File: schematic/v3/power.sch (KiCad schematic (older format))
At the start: 17 parts, among them IC1 MCP73831/2, J13 LIPO_BAT, SW1 RS stock no. 448-0747, U1 TLV71333PDBV, U3 TLV71333PDBV

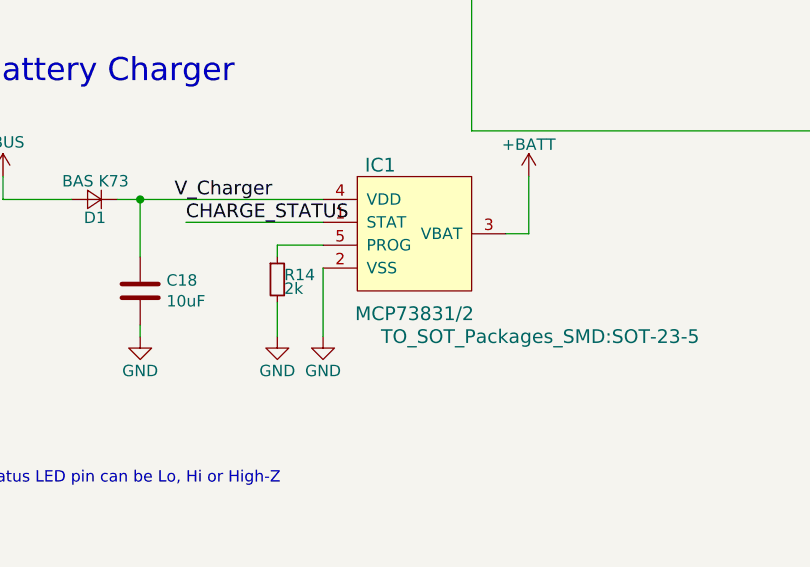
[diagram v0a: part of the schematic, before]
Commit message: Add 4.7uF caps around battery charger
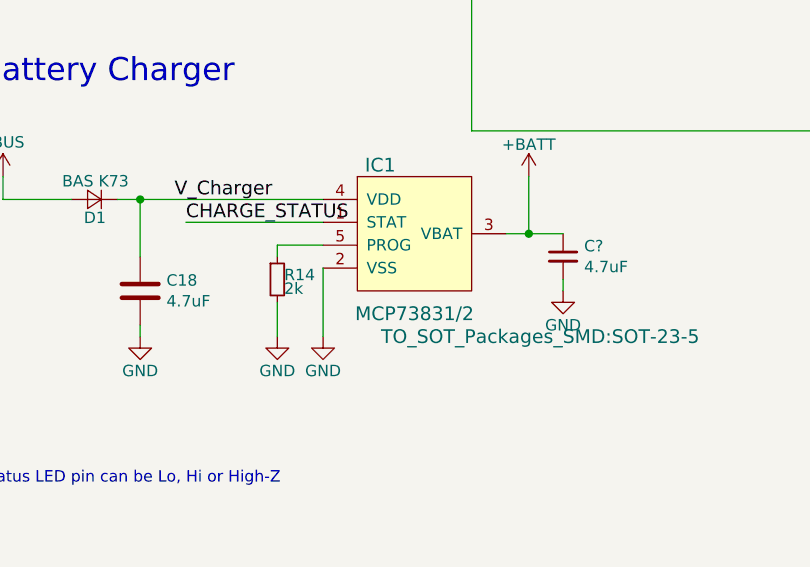
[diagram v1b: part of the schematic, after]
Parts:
- added C?: 4.7uF, symbol Device:C_Small
- C18: value 10uF -> 4.7uF
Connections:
- wire segments 75 -> 77
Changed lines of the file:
@@
 P 2650 4050
 F 0 "C18" H 2765 4096 50  0000 L CNN
-F 1 "10uF" H 2765 4005 50  0000 L CNN
+F 1 "4.7uF" H 2765 4005 50  0000 L CNN
 F 2 "" H 2688 3900 50  0001 C CNN
 F 3 "~" H 2650 4050 50  0001 C CNN
@@
 	4650 1900 4500 1900
 Connection ~ 6850 1850
+$Comp
+L Device:C_Small C?
+U 1 1 5BFBB945
+P 4500 3900
+F 0 "C?" H 4592 3946 50  0000 L CNN
+F 1 "4.7uF" H 4592 3855 50  0000 L CNN
+F 2 "" H 4500 3900 50  0001 C CNN
+F 3 "~" H 4500 3900 50  0001 C CNN
+	1    4500 3900
+	1    0    0    -1
+$EndComp
+Wire Wire Line
+	4350 3800 4500 3800
+Connection ~ 4350 3800
+$Comp
+L gps_node-rescue:GND-power #PWR?
+U 1 1 5BFBD3F1
+P 4500 4050
+F 0 "#PWR?" H 4500 3800 50  0001 C CNN
+F 1 "GND" H 4500 3900 50  0000 C CNN
+F 2 "" H 4500 4050 50  0001 C CNN
+F 3 "" H 4500 4050 50  0001 C CNN
+	1    4500 4050
+	1    0    0    -1
+$EndComp
+Wire Wire Line
+	4500 4050 4500 4000
 $EndSCHEMATC

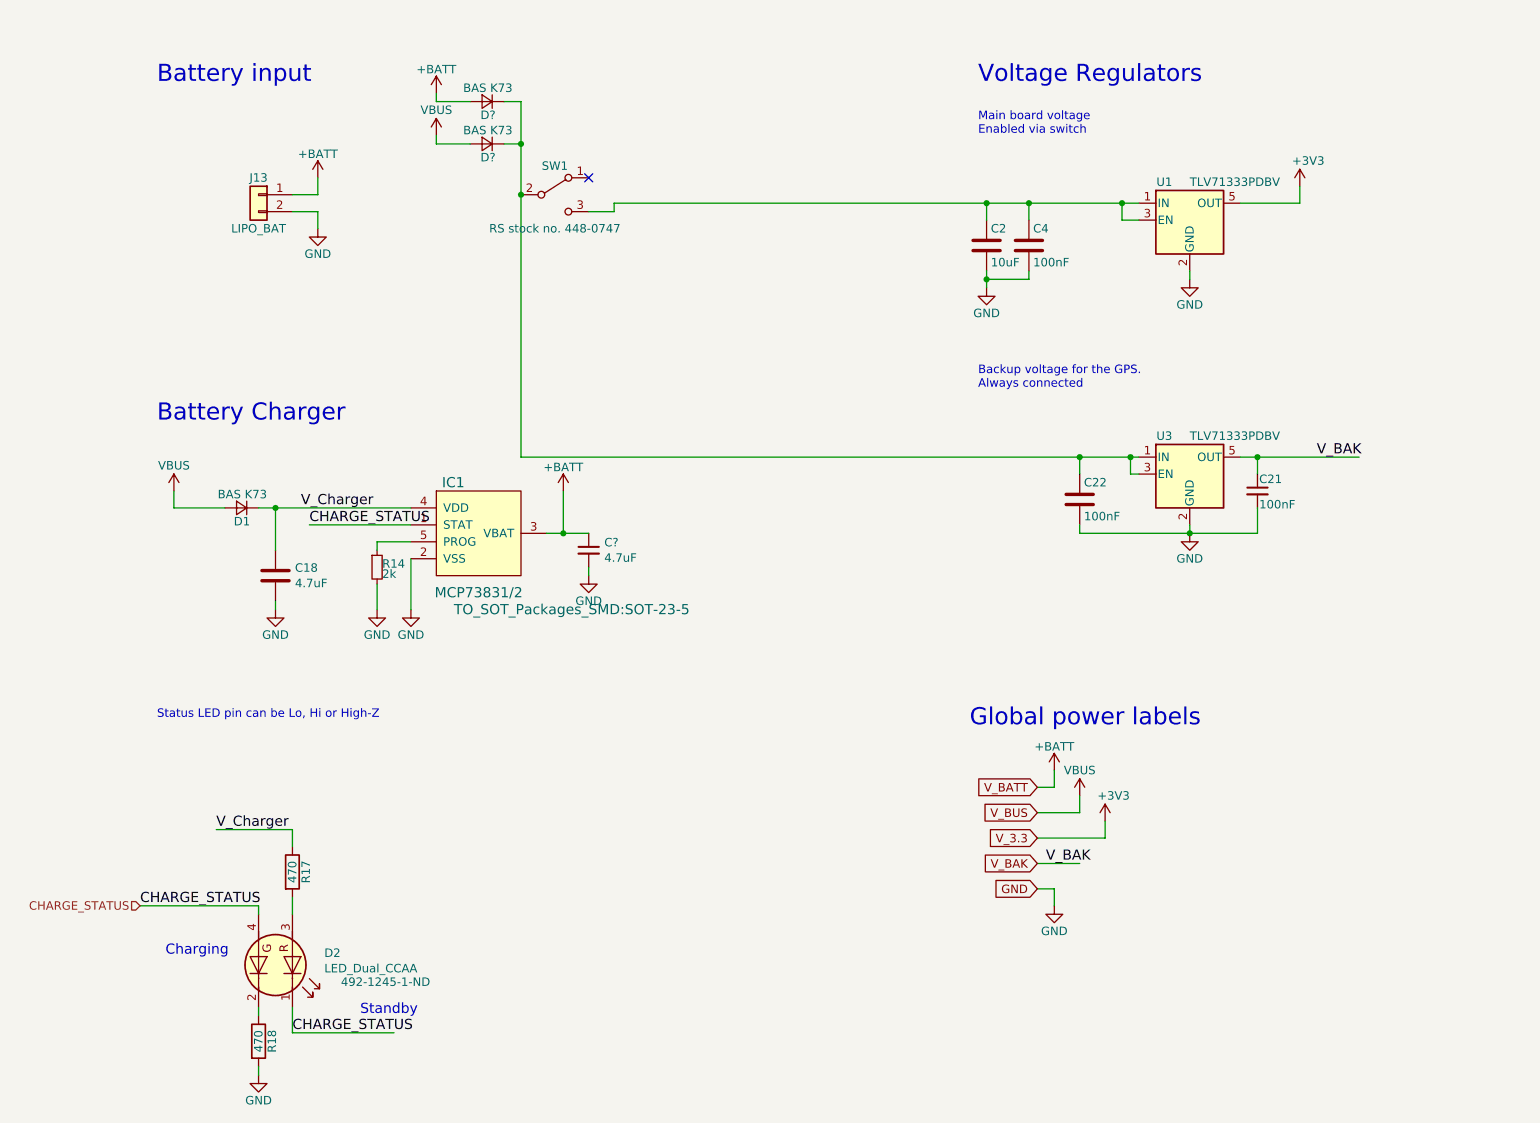
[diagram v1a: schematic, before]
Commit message: Replace 10uF by 4.7uF and clean up power circuit
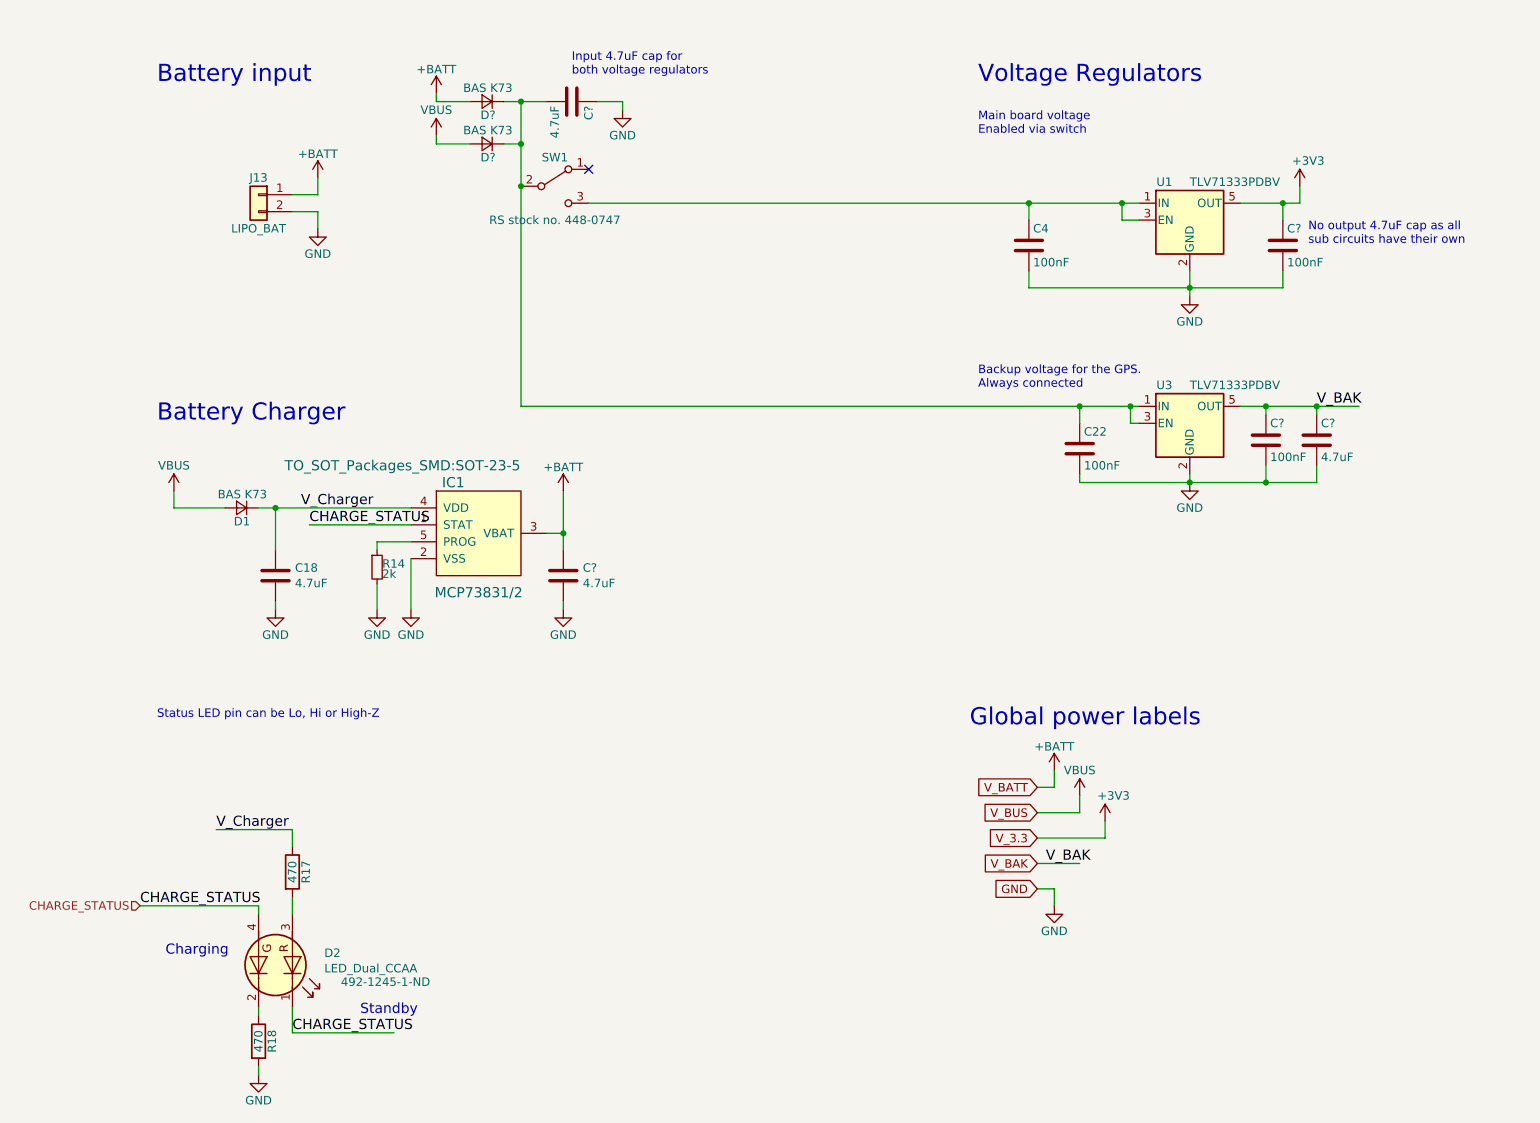
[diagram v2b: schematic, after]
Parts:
- removed C2: 10uF, Capacitors_SMD:C_0805, symbol gps_node-rescue:C
- removed C21: 100nF, Capacitors_SMD:C_0805, symbol gps_node-rescue:C_Small
- removed C?: 4.7uF, symbol Device:C_Small
- added C? (x2): 4.7uF, Capacitors_SMD:C_0805, symbol gps_node-rescue:C
- added C? (x2): 100nF, Capacitors_SMD:C_0805, symbol gps_node-rescue:C
- added C?: 4.7uF, symbol Device:C
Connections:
- wire segments 77 -> 83
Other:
- note added: "Input 4.7uF cap for \nboth voltage regulators"
- note added: "No output 4.7uF cap as all \nsub circuits have their own"
- moved on the sheet: C22, SW1, U3

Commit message: Cleaned up schematic
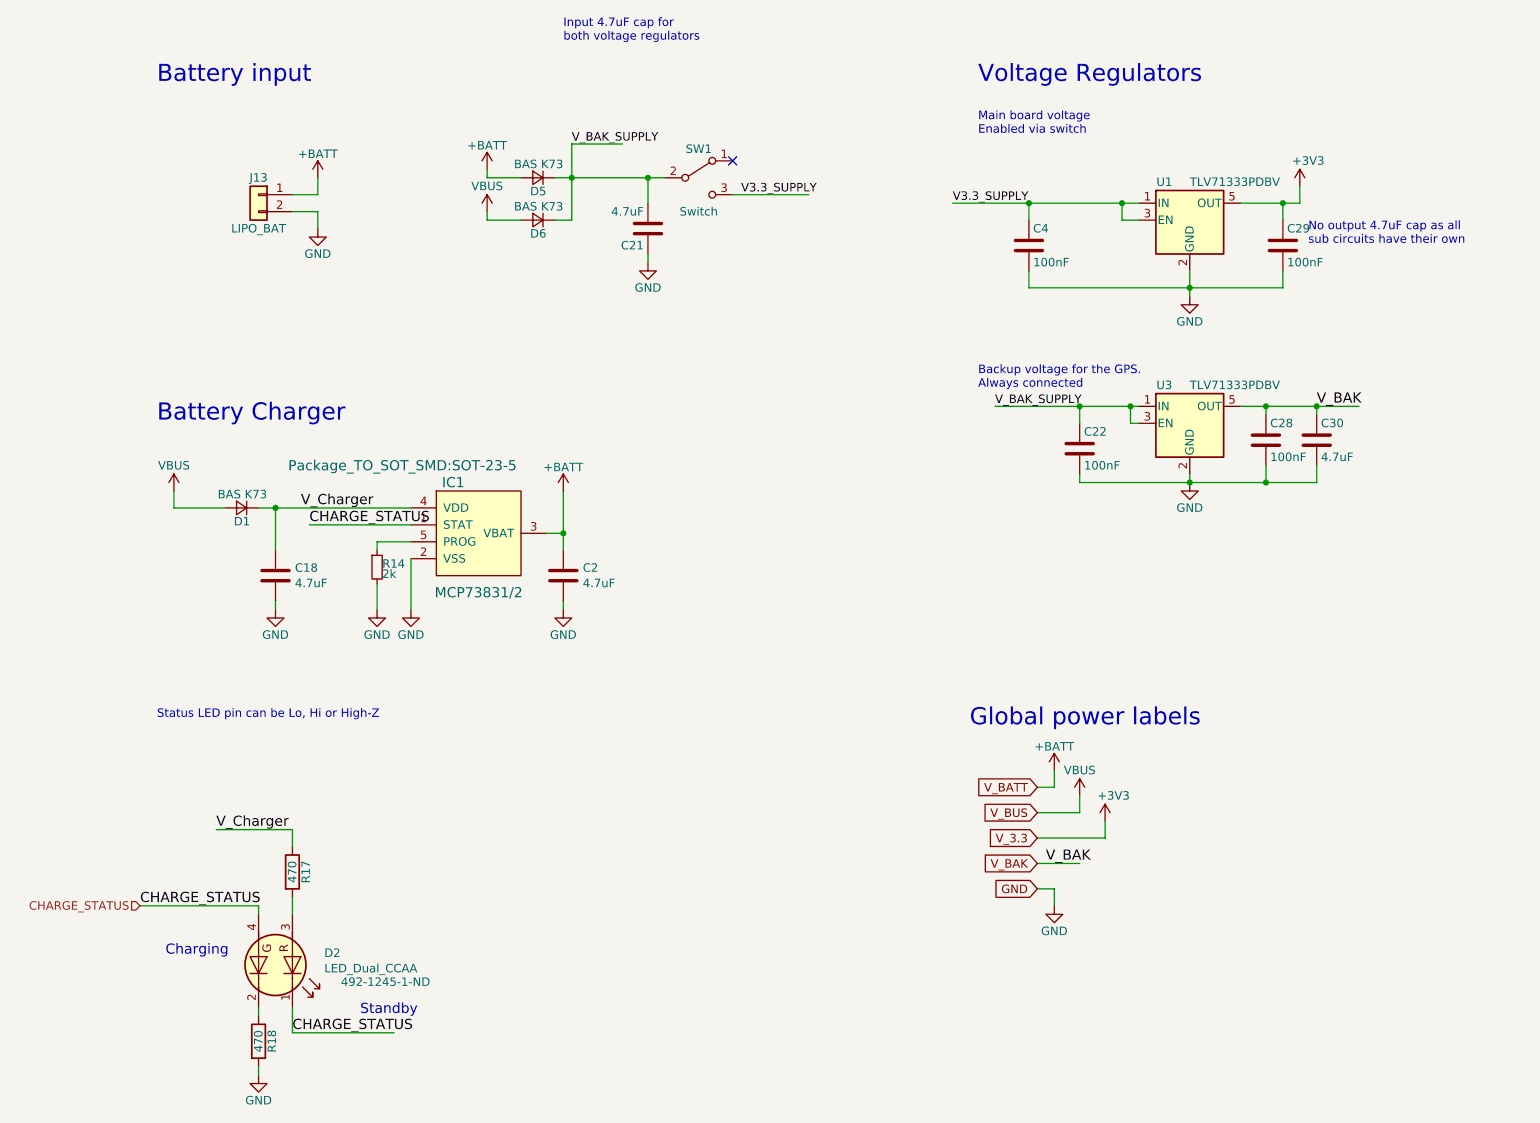
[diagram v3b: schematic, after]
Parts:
- C18: footprint (none) -> Capacitor_SMD:C_0805_2012Metric
- C2: renamed from C?; footprint (none) -> Capacitor_SMD:C_0805_2012Metric
- C21, C28, C29, C30: renamed from C?; footprint Capacitors_SMD:C_0805 -> Capacitor_SMD:C_0805_2012Metric
- C22, C4: footprint Capacitors_SMD:C_0805 -> Capacitor_SMD:C_0805_2012Metric
- D1: footprint Diodes_SMD:D_SOT-23_ANK -> Diode_SMD:D_SOT-23_ANK
- D5, D6: renamed from D?; footprint Diodes_SMD:D_SOT-23_ANK -> Diode_SMD:D_SOT-23_ANK
- IC1, U1, U3: footprint TO_SOT_Packages_SMD:SOT-23-5 -> Package_TO_SOT_SMD:SOT-23-5
- J13: footprint Connectors_Molex:Molex_MicroLatch-53253-0270_02x2.00mm_Straight -> Connector_PinHeader_2.00mm:PinHeader_1x02_P2.00mm_Vertical
- R14, R17, R18: footprint Resistors_SMD:R_0805 -> Resistor_SMD:R_0805_2012Metric
- SW1: value RS stock no. 448-0747 -> Switch; footprint EG1224:EG1224_Switch -> Display_7Segment:MAN3620A
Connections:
- net labels added: V3.3_SUPPLY, V_BAK_SUPPLY
- wire segments 83 -> 85
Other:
- moved on the sheet: C21, D5, D6, SW1

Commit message: Updated layout to revised schematic, moved switch and usb
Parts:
- SW1: footprint Display_7Segment:MAN3620A -> EG1224:EG1224_Switch
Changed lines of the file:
@@
 F 0 "SW1" H 5150 1870 50  0000 C CNN
 F 1 "Switch" H 5150 1500 50  0000 C CNN
-F 2 "Display_7Segment:MAN3620A" H 5150 1700 50  0001 C CNN
+F 2 "EG1224:EG1224_Switch" H 5150 1700 50  0001 C CNN
 F 3 "" H 5150 1700 50  0001 C CNN
 	1    5150 1700
